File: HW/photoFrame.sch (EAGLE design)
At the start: 2 parts, among them U1 NANO

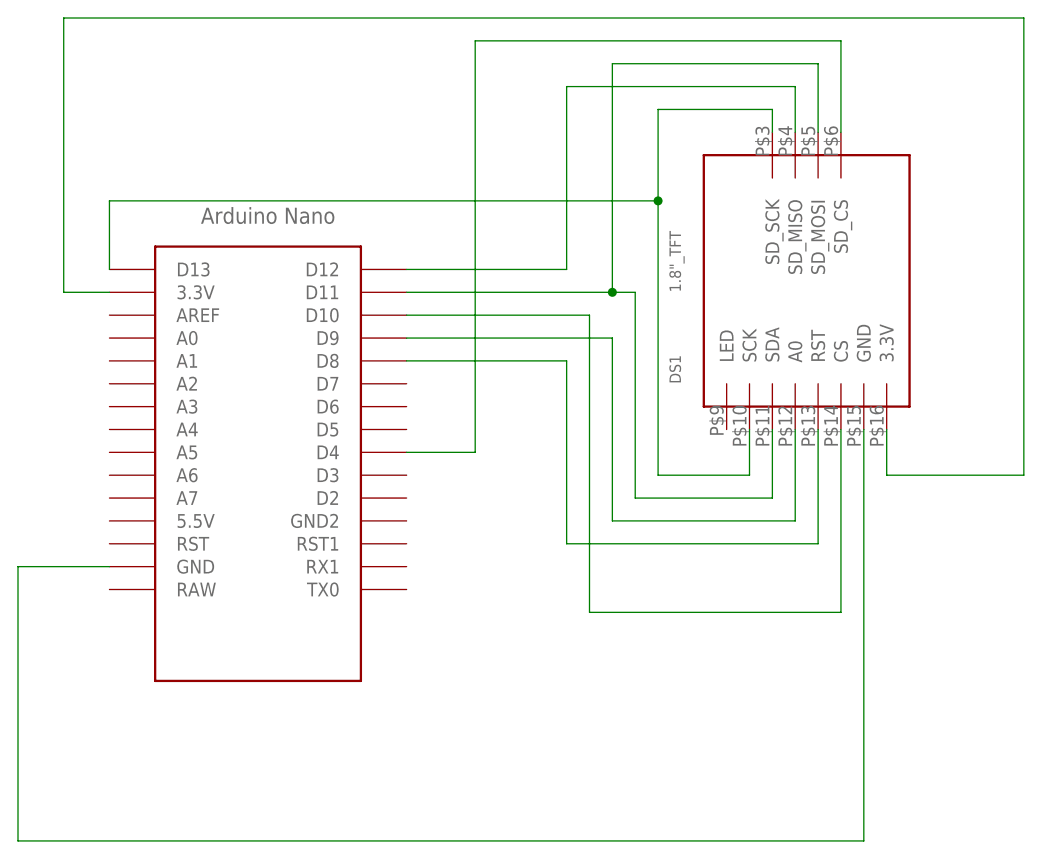
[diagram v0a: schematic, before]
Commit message: Adding Switches on the HW schematics & BOM
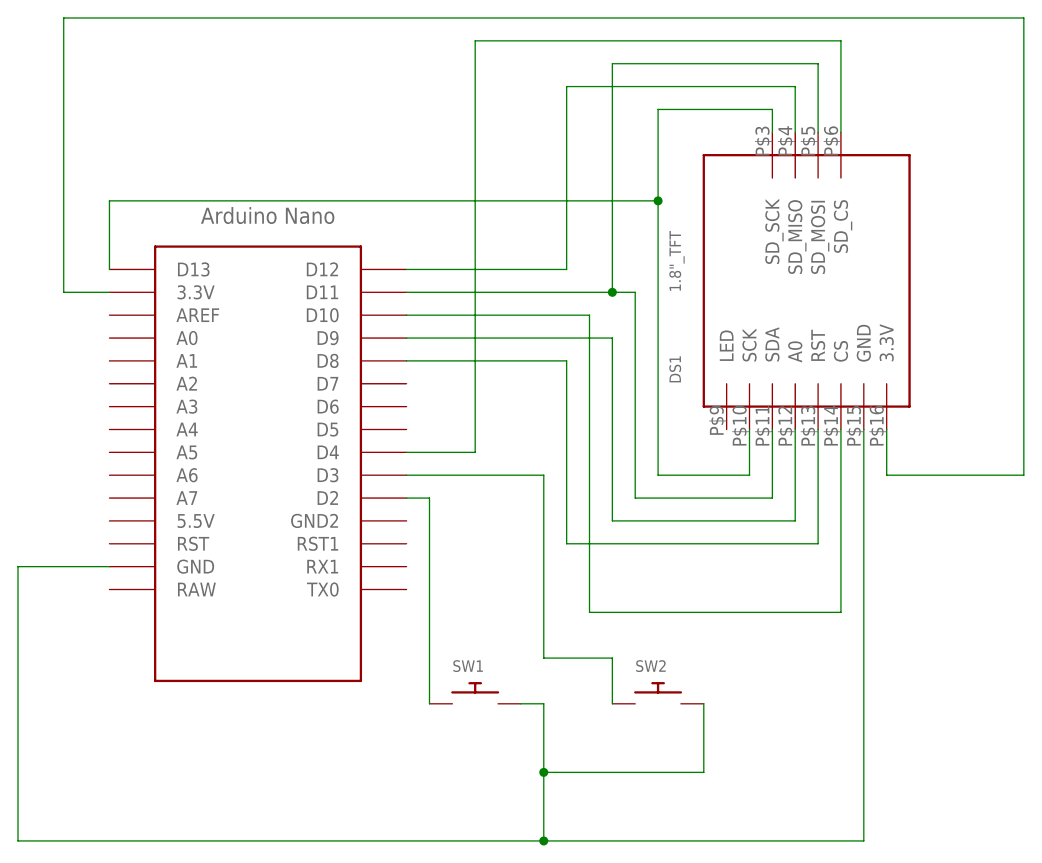
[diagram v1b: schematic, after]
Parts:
- added SW1, SW2: (no value), adafruit:SWITCH_PUSHBUTTONC&K_KSS
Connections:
- new net N$11: SW2.P$1, U1.D3
- new net N$9: SW1.P$1, U1.D2
- net N$2: now also SW1.P$2, SW2.P$2
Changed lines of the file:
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@@
 <layer number="56" name="wert" color="7" fill="1" visible="no" active="no"/>
 <layer number="57" name="tCAD" color="7" fill="1" visible="no" active="no"/>
+<layer number="59" name="tCarbon" color="7" fill="1" visible="no" active="no"/>
+<layer number="60" name="bCarbon" color="7" fill="1" visible="no" active="no"/>
 <layer number="88" name="SimResults" color="9" fill="1" visible="yes" active="yes"/>
 <layer number="89" name="SimProbes" color="9" fill="1" visible="yes" active="yes"/>
@@
 <layer number="113" name="IDFDebug" color="7" fill="1" visible="yes" active="yes"/>
 <layer number="116" name="Patch_BOT" color="7" fill="1" visible="yes" active="yes"/>
+<layer number="118" name="Rect_Pads" color="7" fill="1" visible="no" active="no"/>
 <layer number="121" name="_tsilk" color="7" fill="1" visible="yes" active="yes"/>
 <layer number="122" name="_bsilk" color="7" fill="1" visible="yes" active="yes"/>
@@
 <layer number="127" name="_tValues" color="7" fill="1" visible="yes" active="yes"/>
 <layer number="128" name="_bValues" color="7" fill="1" visible="yes" active="yes"/>
+<layer number="129" name="Mask" color="7" fill="1" visible="yes" active="yes"/>
 <layer number="131" name="tAdjust" color="7" fill="1" visible="yes" active="yes"/>
 <layer number="132" name="bAdjust" color="7" fill="1" visible="yes" active="yes"/>
@@
 <layer number="223" name="223bmp" color="7" fill="1" visible="yes" active="yes"/>
 <layer number="224" name="224bmp" color="7" fill="1" visible="yes" active="yes"/>
+<layer number="225" name="225bmp" color="7" fill="1" visible="yes" active="yes"/>
+<layer number="226" name="226bmp" color="7" fill="1" visible="yes" active="yes"/>
+<layer number="227" name="227bmp" color="7" fill="1" visible="yes" active="yes"/>
+<layer number="228" name="228bmp" color="7" fill="1" visible="yes" active="yes"/>
+<layer number="229" name="229bmp" color="7" fill="1" visible="yes" active="yes"/>
+<layer number="230" name="230bmp" color="7" fill="1" visible="yes" active="yes"/>
+<layer number="231" name="Eagle3D_PG1" color="7" fill="1" visible="no" active="no"/>
+<layer number="232" name="Eagle3D_PG2" color="7" fill="1" visible="no" active="no"/>
+<layer number="233" name="Eagle3D_PG3" color="7" fill="1" visible="no" active="no"/>
 <layer number="248" name="Housing" color="7" fill="1" visible="yes" active="yes"/>
 <layer number="249" name="Edge" color="7" fill="1" visible="yes" active="yes"/>
@@
 <layer number="251" name="SMDround" color="7" fill="1" visible="yes" active="yes"/>
 <layer number="254" name="cooling" color="7" fill="1" visible="yes" active="yes"/>
+<layer number="255" name="routoute" color="7" fill="1" visible="yes" active="yes"/>
 </layers>
 <schematic xreflabel="%F%N/%S.%C%R" xrefpart="/%S.%C%R">
@@
 <part name="U1" library="Arduino-clone" deviceset="NANO" device=""/>
 <part name="DS1" library="tft_1.8_1.44_oled_0.96" deviceset="1.8&quot;_TFT" device=""/>
+<part name="SW1" library="adafruit" library_urn="urn:adsk.eagle:library:420" deviceset="SWITCH_PUSHBUTTON" device="C&amp;K_KSS" package3d_urn="urn:adsk.eagle:package:6240958/1"/>
+<part name="SW2" library="adafruit" library_urn="urn:adsk.eagle:library:420" deviceset="SWITCH_PUSHBUTTON" device="C&amp;K_KSS" package3d_urn="urn:adsk.eagle:package:6240958/1"/>
 </parts>
 <sheets>
@@
 <attribute name="VALUE" x="104.14" y="63.5" size="1.27" layer="96" rot="R90"/>
 </instance>
+<instance part="SW1" gate="G$1" x="81.28" y="17.78" smashed="yes">
+<attribute name="NAME" x="78.74" y="21.336" size="1.27" layer="95"/>
+<attribute name="VALUE" x="78.74" y="15.494" size="1.27" layer="96"/>
+</instance>
+<instance part="SW2" gate="G$1" x="101.6" y="17.78" smashed="yes">
+<attribute name="NAME" x="99.06" y="21.336" size="1.27" layer="95"/>
+<attribute name="VALUE" x="99.06" y="15.494" size="1.27" layer="96"/>
+</instance>
 </instances>
 <busses>
@@
 <pinref part="DS1" gate="G$1" pin="GND"/>
 <wire x1="124.46" y1="48.26" x2="124.46" y2="2.54" width="0.1524" layer="91"/>
-<wire x1="124.46" y1="2.54" x2="30.48" y2="2.54" width="0.1524" layer="91"/>
+<wire x1="124.46" y1="2.54" x2="88.9" y2="2.54" width="0.1524" layer="91"/>
 <pinref part="U1" gate="G$1" pin="GND"/>
+<wire x1="88.9" y1="2.54" x2="30.48" y2="2.54" width="0.1524" layer="91"/>
 <wire x1="30.48" y1="2.54" x2="30.48" y2="33.02" width="0.1524" layer="91"/>
 <wire x1="30.48" y1="33.02" x2="40.64" y2="33.02" width="0.1524" layer="91"/>
+<pinref part="SW1" gate="G$1" pin="P$2"/>
+<wire x1="86.36" y1="17.78" x2="88.9" y2="17.78" width="0.1524" layer="91"/>
+<wire x1="88.9" y1="17.78" x2="88.9" y2="10.16" width="0.1524" layer="91"/>
+<junction x="88.9" y="2.54"/>
+<pinref part="SW2" gate="G$1" pin="P$2"/>
+<wire x1="88.9" y1="10.16" x2="88.9" y2="2.54" width="0.1524" layer="91"/>
+<wire x1="106.68" y1="17.78" x2="106.68" y2="10.16" width="0.1524" layer="91"/>
+<wire x1="106.68" y1="10.16" x2="88.9" y2="10.16" width="0.1524" layer="91"/>
+<junction x="88.9" y="10.16"/>
 </segment>
 </net>
@@
 </segment>
 </net>
+<net name="N$9" class="0">
+<segment>
+<pinref part="U1" gate="G$1" pin="D2"/>
+<pinref part="SW1" gate="G$1" pin="P$1"/>
+<wire x1="73.66" y1="40.64" x2="76.2" y2="40.64" width="0.1524" layer="91"/>
+<wire x1="76.2" y1="40.64" x2="76.2" y2="17.78" width="0.1524" layer="91"/>
+</segment>
+</net>
+<net name="N$11" class="0">
+<segment>
+<pinref part="U1" gate="G$1" pin="D3"/>
+<wire x1="73.66" y1="43.18" x2="88.9" y2="43.18" width="0.1524" layer="91"/>
+<wire x1="88.9" y1="43.18" x2="88.9" y2="22.86" width="0.1524" layer="91"/>
+<wire x1="88.9" y1="22.86" x2="96.52" y2="22.86" width="0.1524" layer="91"/>
+<pinref part="SW2" gate="G$1" pin="P$1"/>
+<wire x1="96.52" y1="22.86" x2="96.52" y2="17.78" width="0.1524" layer="91"/>
+</segment>
+</net>
 </nets>
 </sheet>
@@
 </schematic>
 </drawing>
+<compatibility>
+<note version="8.2" severity="warning">
+Since Version 8.2, EAGLE supports online libraries. The ids
+of those online libraries will not be understood (or retained)
+with this version.
+</note>
+<note version="8.3" severity="warning">
+Since Version 8.3, EAGLE supports URNs for individual library
+assets (packages, symbols, and devices). The URNs of those assets
+will not be understood (or retained) with this version.
+</note>
+<note version="8.3" severity="warning">
+Since Version 8.3, EAGLE supports the association of 3D packages
+with devices in libraries, schematics, and board files. Those 3D
+packages will not be understood (or retained) with this version.
+</note>
+</compatibility>
 </eagle>

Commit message: Adding Led - D7 Connection that was forgotten.
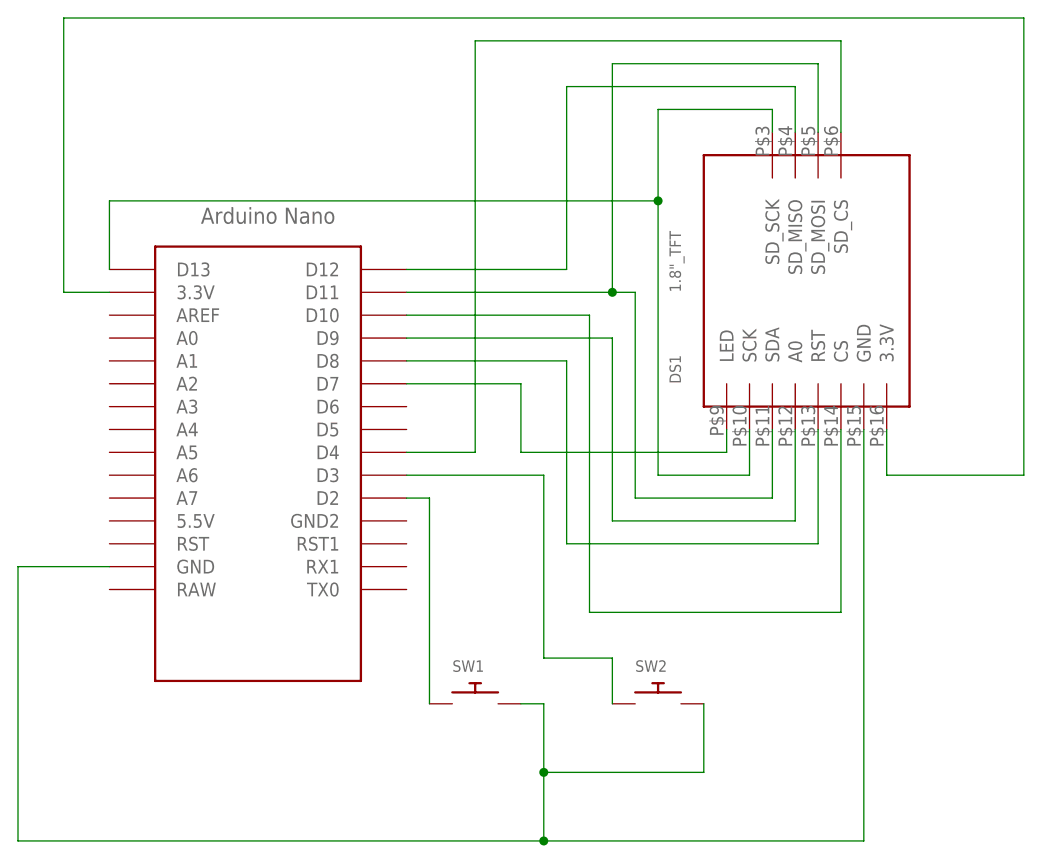
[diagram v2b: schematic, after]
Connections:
- new net N$12: DS1.LED, U1.D7
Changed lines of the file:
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@@
+</segment>
+</net>
+<net name="N$12" class="0">
+<segment>
+<pinref part="DS1" gate="G$1" pin="LED"/>
+<wire x1="109.22" y1="48.26" x2="109.22" y2="45.72" width="0.1524" layer="91"/>
+<wire x1="109.22" y1="45.72" x2="86.36" y2="45.72" width="0.1524" layer="91"/>
+<wire x1="86.36" y1="45.72" x2="86.36" y2="53.34" width="0.1524" layer="91"/>
+<pinref part="U1" gate="G$1" pin="D7"/>
+<wire x1="86.36" y1="53.34" x2="73.66" y2="53.34" width="0.1524" layer="91"/>
 </segment>
 </net>
